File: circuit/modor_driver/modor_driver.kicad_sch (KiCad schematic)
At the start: 15 parts, among them J1 Conn_01x06, J2 Conn_01x04, J3 Conn_01x03, J4 Conn_01x04, SW1 SW_Push, U1 STM32C011F4Px

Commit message: 一旦回路図完成
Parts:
- removed C1: C_Polarized_Small, symbol Device:C_Polarized_Small
- removed H1, H2: MountingHole_Pad_MP, symbol Mechanical:MountingHole_Pad_MP
- added C1: 1u, symbol Device:C_Small
- added C5: 0.1u, symbol Device:C_Small
- added C6: 47u, symbol Device:C_Polarized_Small
- added J2: ZH, symbol Connector_Generic:Conn_01x06
- added J6, J7: XT_pad, symbol Connector_Generic:Conn_01x02
- added U3: ~, symbol Oscillator:SIT2001B
- J1: value Conn_01x06 -> ZH
- J3: renamed from J2; value Conn_01x04 -> PH
- J4: value Conn_01x04 -> XH
- J5: renamed from J3; value Conn_01x03 -> PA
- R1: value R_Small -> 560
- renumbered C3 to C2, C2 to C3
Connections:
- net +3V3: now also C1.1, C5.1, J2.6 (Pin_6), U3.4 (VDD)
- net GND: now also C1.2, C5.2, C6.2, J2.1 (Pin_1), J6.1 (Pin_1), J7.1 (Pin_1), U3.1 (GND)
- net OSC_IN: now also U3.5 (OUT-)
- net SPI_CS: now also J2.5 (Pin_5)
- net SPI_MISO: now also J2.3 (Pin_3)
- net SPI_MOSI: now also J2.4 (Pin_4)
- net SPI_SCK: now also J2.2 (Pin_2)
- net at U2.14 (VIN): now also C6.1, J6.2 (Pin_2), J7.2 (Pin_2)
- net at U2.11 (M1): now also J5.1 (Pin_1); no longer J5.3 (Pin_3)
- net at U2.13 (M3): now also J5.3 (Pin_3); no longer J5.1 (Pin_1)
- no-connect marks 5 -> 6
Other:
- moved on the sheet: C2, C3, C4, D1, J1, J3, J4, J5, R1, SW1, U1, U2

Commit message: pcb
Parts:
- added D1: LED_Small, LED_SMD:LED_0603_1608Metric_Pad1.05x0.95mm_HandSolder, symbol Device:LED_Small
- added J4: PH, Connector_JST:JST_PH_B3B-PH-K_1x03_P2.00mm_Vertical, symbol Connector_Generic:Conn_01x03
- added R1: 560, Resistor_SMD:R_0603_1608Metric_Pad0.98x0.95mm_HandSolder, symbol Device:R_Small
- C1: footprint (none) -> Capacitor_SMD:C_0603_1608Metric_Pad1.08x0.95mm_HandSolder
- C2: renamed from C5; footprint (none) -> Capacitor_SMD:C_0603_1608Metric_Pad1.08x0.95mm_HandSolder
- C3: renamed from C2; footprint (none) -> Capacitor_SMD:C_0603_1608Metric_Pad1.08x0.95mm_HandSolder
- C4: renamed from C3; footprint (none) -> Capacitor_THT:CP_Radial_D5.0mm_P2.00mm
- C5: renamed from C4; footprint (none) -> Capacitor_SMD:C_0603_1608Metric_Pad1.08x0.95mm_HandSolder
- C6: footprint (none) -> Capacitor_THT:CP_Radial_D5.0mm_P2.00mm
- D2: renamed from D1; footprint (none) -> LED_SMD:LED_0603_1608Metric_Pad1.05x0.95mm_HandSolder
- J1, J2: footprint (none) -> Connector_JST:JST_ZH_B6B-ZR_1x06_P1.50mm_Vertical
- J3: value PH -> pogo pin; footprint (none) -> Connector:Pogo_magnet_1x04_P2.54mm
- J5: renamed from J4; footprint (none) -> Connector_JST:JST_XH_B4B-XH-A_1x04_P2.50mm_Vertical
- J6: renamed from J5; footprint (none) -> Connector_JST:JST_PA_1x03
- J7: renamed from J6; footprint (none) -> Connector_AMASS:AMASS_XT30U-M_1x02_P5.0mm_Vertical
- J8: renamed from J7; footprint (none) -> Connector_AMASS:AMASS_XT30U-F_1x02_P5.0mm_Vertical
- R2: renamed from R1; footprint (none) -> Resistor_SMD:R_0603_1608Metric_Pad0.98x0.95mm_HandSolder
- SW1: footprint (none) -> Button_Switch_SMD:SW_SPST_SKQG_WithStem
- U1: renamed from U3; footprint (none) -> Package_TO_SOT_SMD:SOT-23-5_HandSoldering
- U3: renamed from U2; footprint (none) -> Module:SimpleFOCMini
- renumbered U1 to U2
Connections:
- net +3V3: now also R1.1
- net GND: now also D1.1 (K), J4.1 (Pin_1)
- net UART_RX: now also J4.3 (Pin_3)
- net UART_TX: now also J4.2 (Pin_2)
- new net: D1.2 (A), R1.2

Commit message: レイアウト
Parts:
- added D3: LED_Small, LED_SMD:LED_0603_1608Metric_Pad1.05x0.95mm_HandSolder, symbol Device:LED_Small
- added R3: 10k, Resistor_SMD:R_0603_1608Metric_Pad0.98x0.95mm_HandSolder, symbol Device:R_Small
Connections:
- net GND: now also D3.1 (K)
- net +BATT: now reaches C6.1, J7.2 (Pin_2), J8.2 (Pin_2), U3.14 (VIN)
- net +BATT: now also R3.1
- new net: D3.2 (A), R3.2

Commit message: レイアウト変える
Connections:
- net ENCODER_A: now also U2.14 (PA7); no longer U2.1 (PB7)
- net ENCODER_B: now also U2.1 (PB7); no longer U2.14 (PA7)
- net SPI_CS: now also J1.3 (Pin_3), J2.3 (Pin_3); no longer J1.5 (Pin_5), J2.5 (Pin_5)
- net SPI_MISO: now also J1.4 (Pin_4), J2.4 (Pin_4); no longer J1.3 (Pin_3), J2.3 (Pin_3)
- net SPI_MOSI: now also J1.5 (Pin_5), J2.5 (Pin_5); no longer J1.4 (Pin_4), J2.4 (Pin_4)
- net SWCLK: now also J3.3 (Pin_3); no longer J3.2 (Pin_2)
- net SWDIO: now also J3.2 (Pin_2); no longer J3.3 (Pin_3)
- net UART_RX: now also J4.2 (Pin_2); no longer J4.3 (Pin_3)
- net UART_TX: now also J4.3 (Pin_3); no longer J4.2 (Pin_2)
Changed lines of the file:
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@@
 	)
 	(label "ENCODER_B"
+		(at 139.7 102.87 180)
+		(effects
+			(font
+				(size 1.27 1.27)
+			)
+			(justify right bottom)
+		)
+	)
+	(label "ENCODER_A"
 		(at 175.26 105.41 0)
 		(effects
@@
 		)
 	)
-	(label "ENCODER_A"
-		(at 139.7 102.87 180)
-		(effects
-			(font
-				(size 1.27 1.27)
-			)
-			(justify right bottom)
-		)
-	)
 	(label "SPI_MOSI"
-		(at 78.74 59.69 0)
+		(at 78.74 57.15 0)
 		(effects
 			(font
@@
 	)
 	(label "SWDIO"
-		(at 82.55 134.62 0)
+		(at 82.55 137.16 0)
 		(effects
 			(font
@@
 	)
 	(label "SPI_MOSI"
-		(at 78.74 99.06 0)
+		(at 78.74 96.52 0)
 		(effects
 			(font
@@
 	)
 	(label "SPI_MISO"
-		(at 78.74 101.6 0)
+		(at 78.74 99.06 0)
 		(effects
 			(font
@@
 	)
 	(label "UART_RX"
-		(at 82.55 160.02 0)
+		(at 82.55 162.56 0)
 		(effects
 			(font
@@
 	)
 	(label "SPI_CS"
-		(at 78.74 96.52 0)
+		(at 78.74 101.6 0)
 		(effects
 			(font
@@
 	)
 	(label "SWCLK"
-		(at 82.55 137.16 0)
+		(at 82.55 134.62 0)
 		(effects
 			(font
@@
 	)
 	(label "SPI_MISO"
-		(at 78.74 62.23 0)
+		(at 78.74 59.69 0)
 		(effects
 			(font
@@
 	)
 	(label "SPI_CS"
-		(at 78.74 57.15 0)
+		(at 78.74 62.23 0)
 		(effects
 			(font
@@
 	)
 	(label "UART_TX"
-		(at 82.55 162.56 0)
-		(effects
-			(font
+		(at 82.55 160.02 0)
+		(effects
+			(font

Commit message: いったんやりきった
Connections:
- net NRST: now also J3.2 (Pin_2); no longer J3.4 (Pin_4)
- net SPI_CS: now also J1.2 (Pin_2), J2.2 (Pin_2); no longer J1.3 (Pin_3), J2.3 (Pin_3)
- net SPI_SCK: now also J1.3 (Pin_3), J2.3 (Pin_3); no longer J1.2 (Pin_2), J2.2 (Pin_2)
- net SWDIO: now also J3.4 (Pin_4); no longer J3.2 (Pin_2)
- net UART_RX: now also J4.3 (Pin_3); no longer J4.2 (Pin_2)
- net UART_TX: now also J4.2 (Pin_2); no longer J4.3 (Pin_3)
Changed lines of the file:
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@@
 	)
 	(label "NRST"
-		(at 82.55 132.08 0)
+		(at 82.55 137.16 0)
 		(effects
 			(font
@@
 	)
 	(label "SWDIO"
-		(at 82.55 137.16 0)
+		(at 82.55 132.08 0)
 		(effects
 			(font
@@
 	)
 	(label "UART_RX"
-		(at 82.55 162.56 0)
+		(at 82.55 160.02 0)
 		(effects
 			(font
@@
 	)
 	(label "SPI_CS"
-		(at 78.74 101.6 0)
+		(at 78.74 104.14 0)
 		(effects
 			(font
@@
 	)
 	(label "SPI_SCK"
-		(at 78.74 104.14 0)
+		(at 78.74 101.6 0)
 		(effects
 			(font
@@
 	)
 	(label "SPI_CS"
-		(at 78.74 62.23 0)
+		(at 78.74 64.77 0)
 		(effects
 			(font
@@
 	)
 	(label "UART_TX"
-		(at 82.55 160.02 0)
+		(at 82.55 162.56 0)
 		(effects
 			(font
@@
 	)
 	(label "SPI_SCK"
-		(at 78.74 64.77 0)
-		(effects
-			(font
+		(at 78.74 62.23 0)
+		(effects
+			(font

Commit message: いったん完成
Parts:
- removed SW1: SW_Push, Button_Switch_SMD:SW_SPST_SKQG_WithStem, symbol Switch:SW_Push
- added SW1: SW_MEC_5E, Button_Switch_SMD:SKRPACE010, symbol Switch:SW_MEC_5E
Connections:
- net GND: now also SW1.1, SW1.2
- net NRST: now also SW1.3 (K), SW1.4 (A)
- net SWCLK: now also J3.4 (Pin_4); no longer J3.3 (Pin_3)
- net SWDIO: now also J3.3 (Pin_3); no longer J3.4 (Pin_4)
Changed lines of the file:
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@@
 	)
 	(junction
+		(at 130.81 55.88)
+		(diameter 0)
+		(color 0 0 0 0)
+	)
+	(junction
 		(at 109.22 154.94)
 		(diameter 0)
@@
 		(color 0 0 0 0)
 	)
+	(junction
+		(at 130.81 66.04)
+		(diameter 0)
+		(color 0 0 0 0)
+	)
 	(no_connect
 		(at 114.3 157.48)
@@
 	(wire
 		(pts
+			(xy 128.27 55.88) (xy 130.81 55.88)
+		)
+		(stroke
+			(width 0)
+			(type default)
+		)
+	)
+	(wire
+		(pts
 			(xy 96.52 72.39) (xy 87.63 72.39)
 		)
@@
 	(wire
 		(pts
+			(xy 128.27 66.04) (xy 130.81 66.04)
+		)
+		(stroke
+			(width 0)
+			(type default)
+		)
+	)
+	(wire
+		(pts
 			(xy 219.71 102.87) (xy 219.71 116.84)
 		)
@@
 	)
 	(label "SWDIO"
-		(at 82.55 132.08 0)
+		(at 82.55 134.62 0)
 		(effects
 			(font
@@
 	)
 	(label "SWCLK"
-		(at 82.55 134.62 0)
+		(at 82.55 132.08 0)
 		(effects
 			(font
@@
 	)
 	(symbol
-		(lib_id "Switch:SW_Push")
-		(at 130.81 60.96 90)
-		(unit 1)
-		(exclude_from_sim no)
-		(in_bom yes)
-		(on_board yes)
-		(dnp no)
-		(fields_autoplaced yes)
-		(property "Reference" "SW1"
-			(at 132.08 59.6899 90)
-			(effects
-				(font
-					(size 1.27 1.27)
-				)
-				(justify right)
-			)
-		)
-		(property "Value" "SW_Push"
-			(at 132.08 62.2299 90)
-			(effects
-				(font
-					(size 1.27 1.27)
-				)
-				(justify right)
-			)
-		)
-		(property "Footprint" "Button_Switch_SMD:SW_SPST_SKQG_WithStem"
-			(at 125.73 60.96 0)
-			(effects
-				(font
-					(size 1.27 1.27)
-				)
-				(hide yes)
-			)
-		)
-		(property "Datasheet" "~"
-			(at 125.73 60.96 0)
-			(effects
-				(font
-					(size 1.27 1.27)
-				)
-				(hide yes)
-			)
-		)
-		(property "Description" "Push button switch, generic, two pins"
-			(at 130.81 60.96 0)
-			(effects
-				(font
-					(size 1.27 1.27)
-				)
-				(hide yes)
-			)
-		)
-		(pin "2"
-		)
-		(pin "1"
-		)
-		(instances
-			(project ""
-				(path "/3e392b6a-3aba-468a-ae42-54ab3af6280c"
-					(reference "SW1")
-					(unit 1)
-				)
-			)
-		)
-	)
-	(symbol
 		(lib_id "power:+3V3")
 		(at 157.48 76.2 0)
@@
 					(unit 1)
 				)
+			)
+		)
+	)
+	(symbol
+		(lib_id "Switch:SW_MEC_5E")
+		(at 130.81 60.96 90)
+		(unit 1)
+		(exclude_from_sim no)
+		(in_bom yes)
+		(on_board yes)
+		(dnp no)
+		(fields_autoplaced yes)
+		(property "Reference" "SW1"
+			(at 132.08 59.6899 90)
+			(effects
+				(font
+					(size 1.27 1.27)
+				)
+				(justify right)
+			)
+		)
+		(property "Value" "SW_MEC_5E"
+			(at 132.08 62.2299 90)
+			(effects
+				(font
+					(size 1.27 1.27)
+				)
+				(justify right)
+			)
+		)
+		(property "Footprint" "Button_Switch_SMD:SKRPACE010"
+			(at 123.19 60.96 0)
+			(effects
+				(font
+					(size 1.27 1.27)
+				)
+				(hide yes)
+			)
+		)
+		(property "Datasheet" "http://www.apem.com/int/index.php?controller=attachment&id_attachment=1371"
+			(at 123.19 60.96 0)
+			(effects
+				(font
+					(size 1.27 1.27)
+				)
+				(hide yes)
+			)
+		)
+		(property "Description" "MEC 5E single pole normally-open tactile switch"
+			(at 130.81 60.96 0)
+			(effects
+				(font
+					(size 1.27 1.27)
+				)
+				(hide yes)
+			)
+		)
+		(pin "1"
+		)
+		(pin "2"
+		)
+		(pin "4"
+		)
+		(pin "3"
+		)
+		(instances
+			(project ""
+				(path "/3e392b6a-3aba-468a-ae42-54ab3af6280c"
+					(reference "SW1")
+					(unit 1)
+				)

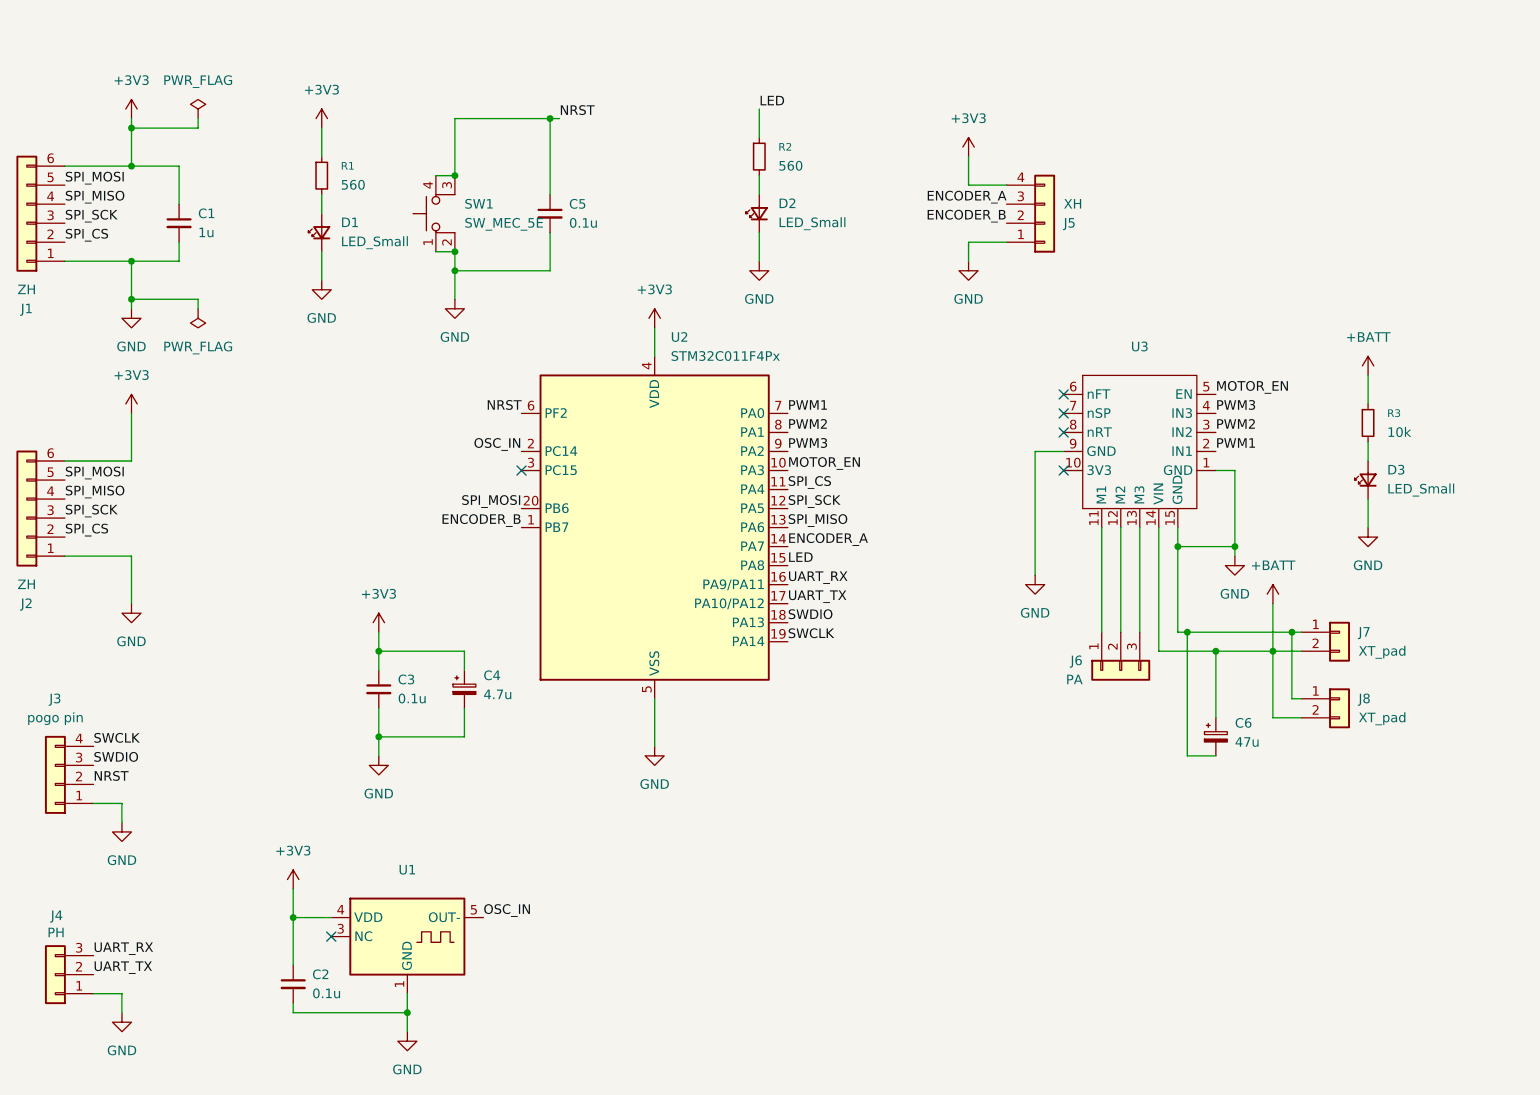
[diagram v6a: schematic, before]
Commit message: コネクタ変更とsimplefocminiを修正
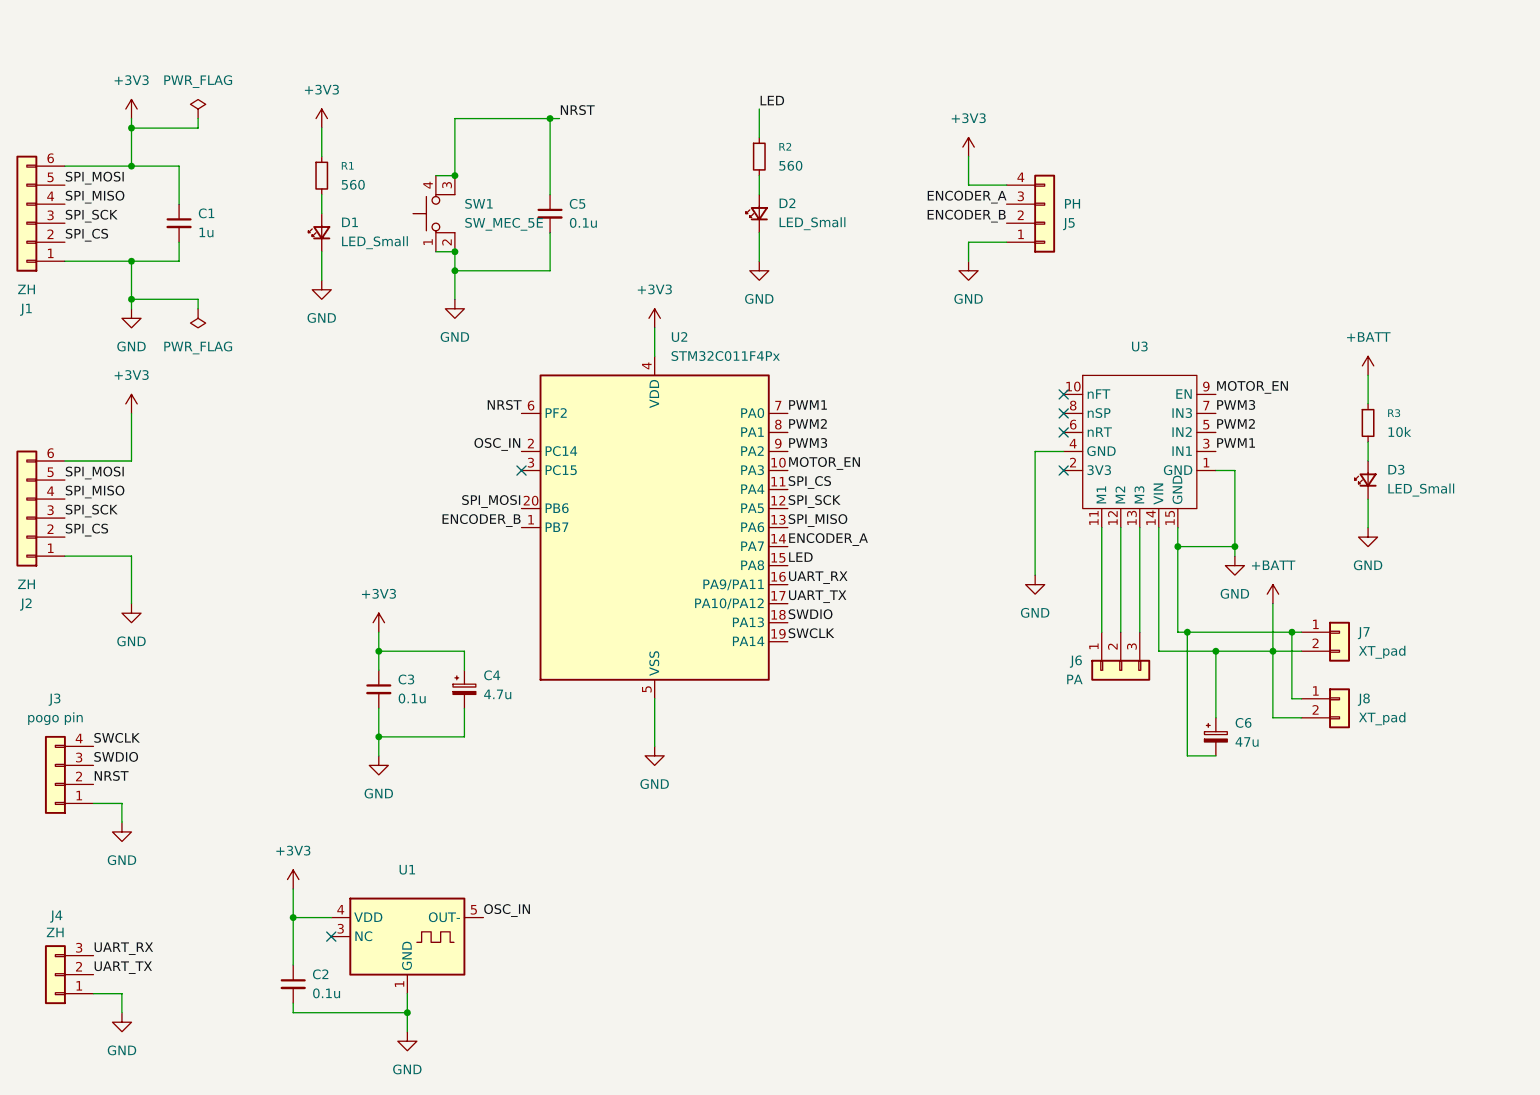
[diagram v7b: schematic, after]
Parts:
- J4: value PH -> ZH; footprint Connector_JST:JST_PH_B3B-PH-K_1x03_P2.00mm_Vertical -> Connector_JST:JST_ZH_B3B-ZR_1x03_P1.50mm_Vertical
- J5: value XH -> PH; footprint Connector_JST:JST_XH_B4B-XH-A_1x04_P2.50mm_Vertical -> Connector_JST:JST_PH_B4B-PH-K_1x04_P2.00mm_Vertical
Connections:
- net GND: now also U3.4 (GND); no longer U3.9 (GND)
- net MOTOR_EN: now also U3.9 (EN); no longer U3.5 (EN)
- net PWM1: now also U3.3 (IN1); no longer U3.2 (IN1)
- net PWM2: now also U3.5 (IN2); no longer U3.3 (IN2)
- net PWM3: now also U3.7 (IN3); no longer U3.4 (IN3)
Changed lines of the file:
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@@
 			)
 		)
-		(property "Value" "PH"
+		(property "Value" "ZH"
 			(at 78.74 156.972 0)
 			(effects
@@
 			)
 		)
-		(property "Footprint" "Connector_JST:JST_PH_B3B-PH-K_1x03_P2.00mm_Vertical"
+		(property "Footprint" "Connector_JST:JST_ZH_B3B-ZR_1x03_P1.50mm_Vertical"
 			(at 77.47 162.56 0)
 			(effects
@@
 			)
 		)
-		(property "Value" "XH"
+		(property "Value" "PH"
 			(at 212.09 59.6901 0)
 			(effects
@@
 			)
 		)
-		(property "Footprint" "Connector_JST:JST_XH_B4B-XH-A_1x04_P2.50mm_Vertical"
+		(property "Footprint" "Connector_JST:JST_PH_B4B-PH-K_1x04_P2.00mm_Vertical"
 			(at 209.55 62.23 0)
 			(effects
